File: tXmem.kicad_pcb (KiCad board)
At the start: 2 copper layers, 39 x 65 mm, 37 parts, among them U1 74LCX125, U10 SPIMEMORY, U11 SPIMEMORY, U12 SPIMEMORY, U13 SPIMEMORY, U14 SPIMEMORY, U15 SPIMEMORY, U16 SPIMEMORY, U17 SPIMEMORY, U18 SPIMEMORY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

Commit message: work in progress
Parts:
- removed XB?1: XBEE, tXmem:XBee
- added XB1: XBEE, tXmem:XBee, F.Cu at (102.3, 112.8)
- moved C1 21.4 mm to (136.0, 80.0)
- moved C13 21.4 mm to (136.0, 110.0)
- moved C5 21.4 mm to (136.0, 90.0)
- moved C9 21.4 mm to (136.0, 100.0)
- moved U13 21.4 mm to (135.0, 85.0)
- moved U17 21.4 mm to (135.0, 75.0)
- moved U5 21.4 mm to (135.0, 105.0)
- moved U9 21.4 mm to (135.0, 95.0)
- moved C11 2.70 mm to (87.7, 71.0)
- moved C15 2.70 mm to (87.7, 61.0)
- moved C3 2.70 mm to (87.7, 91.0)
- moved C7 2.70 mm to (87.7, 81.0)
- moved U10 2.70 mm to (88.7, 86.0)
- moved U14 2.70 mm to (88.7, 76.0)
- moved U18 2.70 mm to (88.7, 66.0)
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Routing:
- net GND: track 248.3 -> 178.2 mm, vias 5 -> 4
- net /SI: track 179.9 -> 115.8 mm
- net /SO: track 168.6 -> 106.5 mm
- net /SCK: track 183.4 -> 122.6 mm
- net /D12: track 47.1 -> 0.00 mm
- net /D11: track 41.1 -> 0.00 mm
- net /D10: track 31.3 -> 0.00 mm
- net /D9: track 21.4 -> 0.00 mm
- net VCC: track 257.6 -> 237.8 mm, vias 2 -> 4
- net /A1: track 39.1 -> 23.1 mm
- net /D15: track 19.7 -> 6.99 mm
- net /A3: track 45.6 -> 34.4 mm
- net /D14: track 26.6 -> 17.4 mm
- net /D13: track 36.6 -> 27.6 mm
- net /~CS: track 47.7 -> 39.1 mm
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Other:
- net class Default: via_drill 0.4 -> 0.2
- rule via_min_drill: 0.3 -> 0.18

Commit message: dwarfing!
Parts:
- moved C1 24.4 mm to (114.2, 69.0)
- moved C5 24.4 mm to (114.2, 79.0)
- moved C9 24.4 mm to (114.2, 89.0)
- moved U13 24.4 mm to (113.2, 74.0)
- moved U17 24.4 mm to (113.2, 64.0)
- moved U5 24.4 mm to (113.2, 94.0)
- moved U9 24.4 mm to (113.2, 84.0)
- moved C13 24.0 mm to (114.9, 98.6)
- moved U3 4.47 mm to (90.0, 108.0)
- moved C10 2.24 mm to (104.0, 69.0)
- moved C2 2.24 mm to (104.0, 89.0)
- moved C6 2.24 mm to (104.0, 79.0)
- moved U12 2.24 mm to (105.0, 74.0)
- moved U16 2.24 mm to (105.0, 64.0)
- moved U4 2.24 mm to (105.0, 94.0)
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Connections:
- net Net-(U1-Pad2) renamed /~E
- XB1 pad 15: (no net) -> Net-(XB1-Pad15)
- XB1 pad 17: (no net) -> Net-(XB1-Pad17)
- XB1 pad 19: (no net) -> Net-(XB1-Pad19)
- XB1 pad 2: (no net) -> Net-(XB1-Pad2)
- XB1 pad 20: (no net) -> Net-(XB1-Pad20)
- XB1 pad 3: (no net) -> Net-(XB1-Pad3)
- XB1 pad 7: (no net) -> Net-(XB1-Pad7)
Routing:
- net /SO: track 106.5 -> 167.3 mm
- net /SI: track 115.8 -> 175.6 mm
- net /SCK: track 122.6 -> 178.4 mm
- net /D12: track 0.00 -> 47.1 mm
- net GND: track 178.2 -> 223.2 mm, vias 4 -> 6
- net /D11: track 0.00 -> 41.3 mm
- net /D10: track 0.00 -> 31.4 mm
- net /D9: track 0.00 -> 21.5 mm
- net VCC: track 237.8 -> 250.8 mm, vias 4 -> 5
- net /A1: track 23.1 -> 35.1 mm, vias 0 -> 1
- net /A0: track 42.6 -> 30.8 mm
- net /D13: track 27.6 -> 36.7 mm
- net /D14: track 17.4 -> 25.4 mm
- net /D15: track 6.99 -> 14.7 mm
- net /D8: track 10.4 -> 17.4 mm
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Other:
- board size 39 x 65 mm -> 35 x 67 mm

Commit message: test fab v1.0
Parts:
- C1, C10, C11, C12, C13, C14, C15, C16, C2, C3, C4, C5, C6, C7, C8, C9: value 104M -> C104M
- R1: value 103J -> R103J
- moved XB1 22.4 mm to (98.3, 134.8)
- moved C14 22.4 mm to (99.8, 81.4)
- moved C1 22.4 mm to (110.2, 91.0)
- moved C10 22.4 mm to (100.0, 91.0)
- moved C11 22.4 mm to (83.8, 91.0)
- moved C12 22.4 mm to (94.0, 111.0)
- moved C13 22.4 mm to (110.9, 120.6)
- moved C15 22.4 mm to (83.6, 81.5)
- moved C16 22.4 mm to (94.0, 121.0)
- moved C2 22.4 mm to (100.0, 111.0)
- moved C3 22.4 mm to (83.8, 111.0)
- moved C4 22.4 mm to (94.0, 91.0)
- moved C5 22.4 mm to (110.2, 101.0)
- moved C6 22.4 mm to (100.0, 101.0)
- moved C7 22.4 mm to (83.8, 101.0)
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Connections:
- XB1 pad 15: Net-(XB1-Pad15) -> (no net)
- XB1 pad 17: Net-(XB1-Pad17) -> (no net)
- XB1 pad 19: Net-(XB1-Pad19) -> (no net)
- XB1 pad 2: Net-(XB1-Pad2) -> (no net)
- XB1 pad 20: Net-(XB1-Pad20) -> (no net)
- XB1 pad 3: Net-(XB1-Pad3) -> (no net)
- XB1 pad 7: Net-(XB1-Pad7) -> (no net)
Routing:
- net /A1: track 35.1 -> 39.8 mm, vias 1 -> 0
- net GND: track 223.2 -> 221.1 mm
- net VCC: track 250.8 -> 248.9 mm
- net /~CS: track 43.4 -> 45.2 mm, vias 3 -> 2
- net /A0: track 30.8 -> 29.5 mm
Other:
- board size 35 x 67 mm -> 35 x 68 mm

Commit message: fix mask clearance and paste clearance
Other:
- rule pad_to_mask_clearance: 0.2 -> 0.1
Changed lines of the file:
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@@
     (pad_size 1.524 1.524)
     (pad_drill 0.762)
-    (pad_to_mask_clearance 0.2)
+    (pad_to_mask_clearance 0.1)
+    (pad_to_paste_clearance -0.05)
     (aux_axis_origin 0 0)
     (grid_origin 80 80)

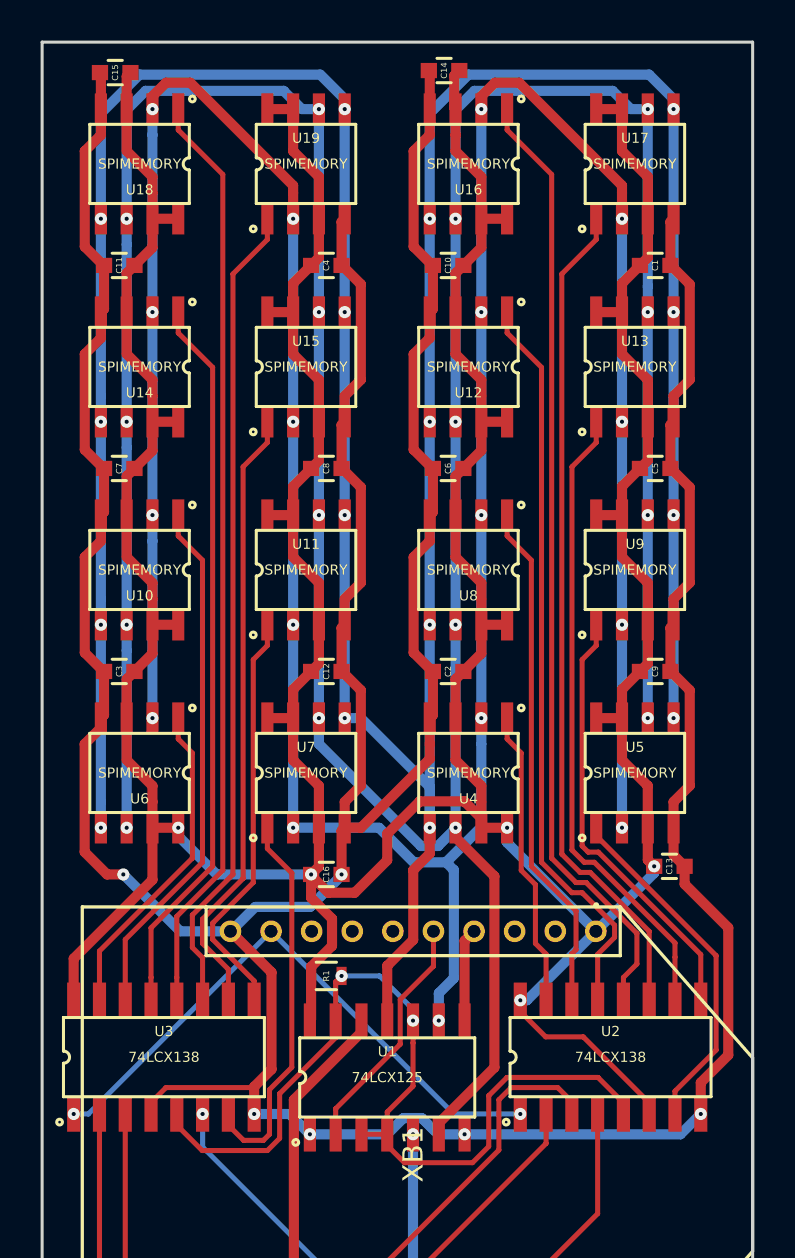
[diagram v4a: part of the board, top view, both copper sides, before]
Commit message: * usegerberextensions false * via drill from 0.2 to 0.18
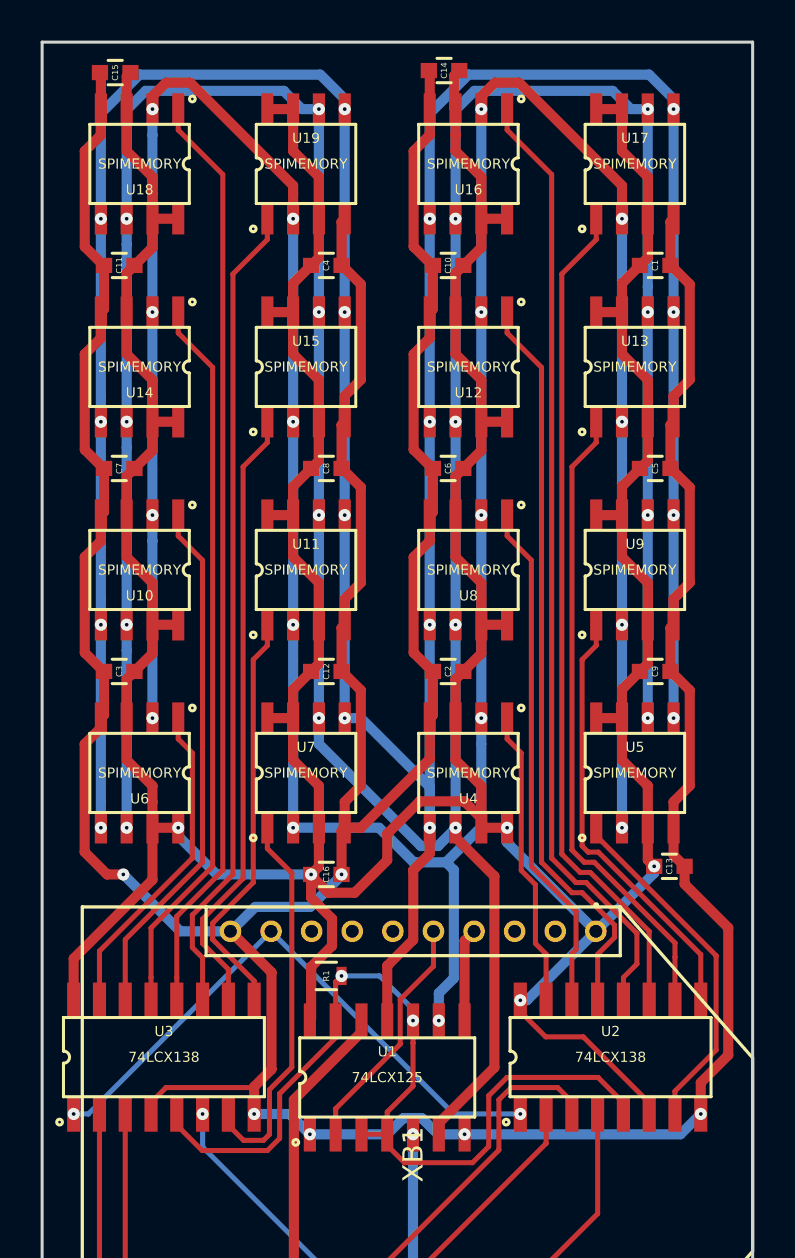
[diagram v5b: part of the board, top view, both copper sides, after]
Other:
- net class Default: via_drill 0.2 -> 0.18

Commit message: minor fix
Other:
- rule pad_to_mask_clearance: 0.1 -> 0
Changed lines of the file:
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@@
-(kicad_pcb (version 4) (host pcbnew 0.201508210901+6109~28~ubuntu14.04.1-product)
+(kicad_pcb (version 4) (host pcbnew 0.201509020901+6148~28~ubuntu14.04.1-product)
   (general
     (links 188)
@@
   )
   (setup
-    (last_trace_width 0.5)
+    (last_trace_width 0.25)
     (user_trace_width 0.5)
     (trace_clearance 0.2)
@@
     (pad_size 1.524 1.524)
     (pad_drill 0.762)
-    (pad_to_mask_clearance 0.1)
-    (pad_to_paste_clearance -0.05)
+    (pad_to_mask_clearance 0)
+    (pad_to_paste_clearance_ratio -0.1)
     (aux_axis_origin 0 0)
     (grid_origin 80 80)
@@
   (module tXmem:XBee (layer F.Cu)
     (at 98.277 134.8 270)
-    (fp_text reference XB1 (at 0 0 450) (layer F.SilkS)
+    (fp_text reference XB1 (at 1.2 0.007 540) (layer F.SilkS)
       (effects (font (size 1 1) (thickness 0.15)))
     )
-    (fp_text value XBEE (at 0 0 450) (layer B.SilkS)
+    (fp_text value XBEE (at 1.1 0.007 540) (layer B.SilkS)
       (effects (font (size 1 1) (thickness 0.15)) (justify mirror))
     )
